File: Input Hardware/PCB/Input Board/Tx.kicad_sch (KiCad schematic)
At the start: 40 parts, among them U1001 TPIC6595, U1002 TPIC6595, U1003 TPIC6595, U1004 TPIC6595

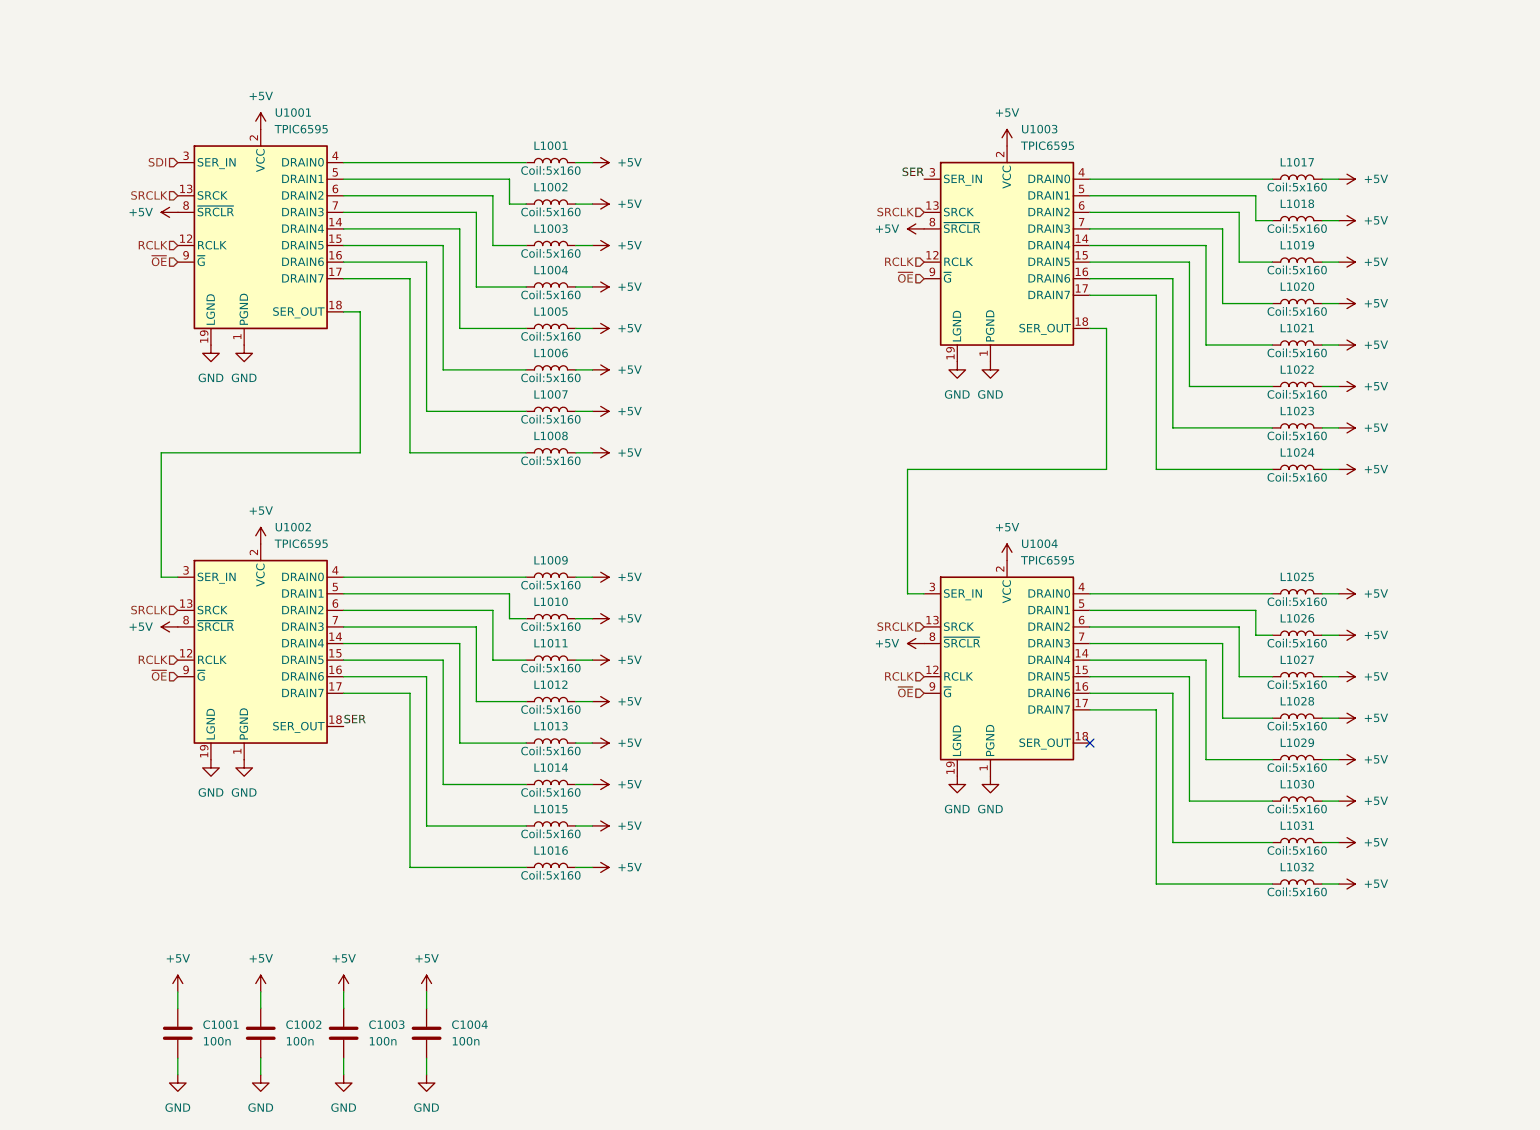
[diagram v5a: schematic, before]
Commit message: driver format update
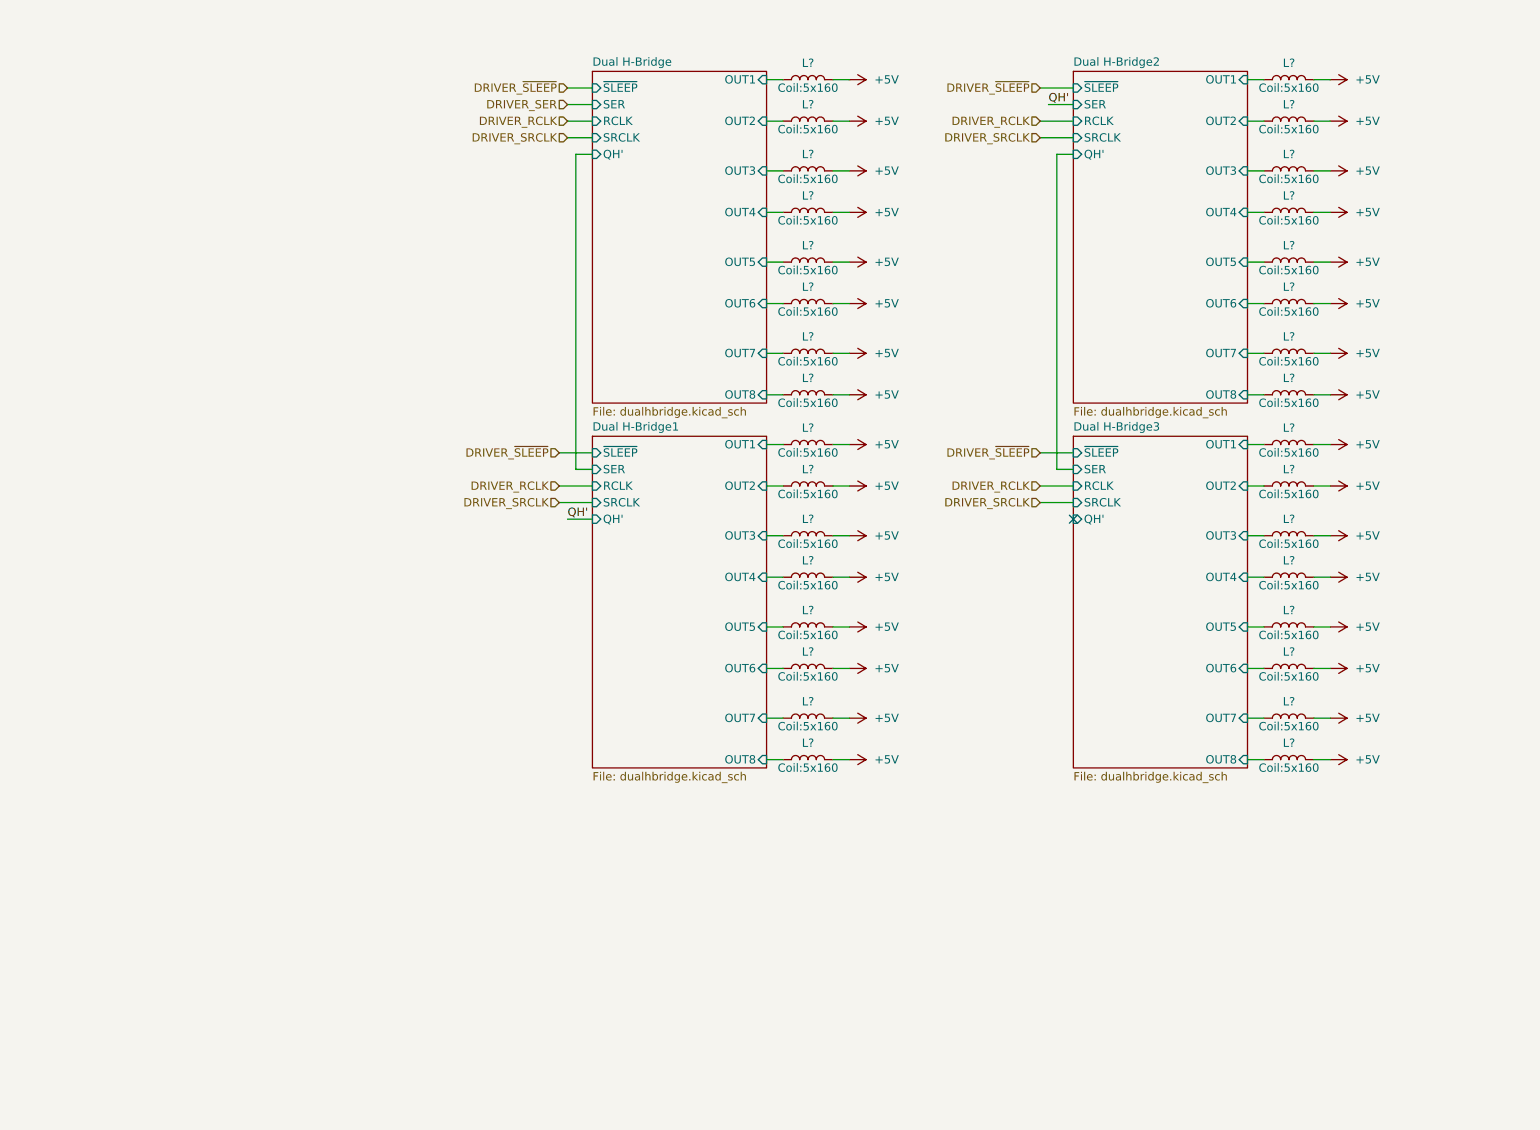
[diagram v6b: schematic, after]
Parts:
- removed C1001, C1002, C1003, C1004: 100n, Capacitor_SMD:C_0603_1608Metric, symbol Device:C
- removed U1001, U1002, U1003, U1004: TPIC6595, Package_SO:SOIC-20W_7.5x12.8mm_P1.27mm, symbol Interface_Expansion:TPIC6595
- renumbered L1019 to L?, L1024 to L?, L1006 to L?, L1003 to L?, L1008 to L?, L1027 to L?, L1007 to L?, L1030 to L?, L1026 to L?, L1004 to L?, L1013 to L?, L1014 to L?, L1011 to L?, L1017 to L?, L1010 to L?, L1031 to L?, L1002 to L?, L1001 to L?, L1005 to L?, L1020 to L?, L1015 to L?, L1023 to L?, L1016 to L?, L1022 to L?, L1018 to L?, L1029 to L?, L1025 to L?, L1028 to L?, L1012 to L?, L1032 to L?, L1009 to L?, L1021 to L?
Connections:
- net Dual H-Bridge2/OUT3: now reaches L?.1
- net Dual H-Bridge2/OUT8: now reaches L?.1
- net Dual H-Bridge/OUT6: now reaches L?.1
- net Dual H-Bridge/OUT3: now reaches L?.1
- net Dual H-Bridge/OUT8: now reaches L?.1
- net Dual H-Bridge3/OUT3: now reaches L?.1
- net Dual H-Bridge/OUT7: now reaches L?.1
- net Dual H-Bridge3/OUT6: now reaches L?.1
- net Dual H-Bridge3/OUT2: now reaches L?.1
- net Dual H-Bridge/OUT4: now reaches L?.1
- net Dual H-Bridge1/OUT5: now reaches L?.1
- net Dual H-Bridge1/OUT6: now reaches L?.1
- net Dual H-Bridge1/OUT3: now reaches L?.1
- net Dual H-Bridge2/OUT1: now reaches L?.1
- net Dual H-Bridge1/OUT2: now reaches L?.1
- net Dual H-Bridge3/OUT7: now reaches L?.1
- net Dual H-Bridge/OUT2: now reaches L?.1
- net Dual H-Bridge2/OUT5: now reaches L?.1
- net Dual H-Bridge2/OUT6: now reaches L?.1
- net Dual H-Bridge2/OUT7: now reaches L?.1
- net Dual H-Bridge2/OUT2: now reaches L?.1
- net Dual H-Bridge2/OUT4: now reaches L?.1
- net Dual H-Bridge/OUT1: now reaches L?.1
- net Dual H-Bridge/OUT5: now reaches L?.1
- net Dual H-Bridge1/OUT7: now reaches L?.1
- net Dual H-Bridge1/OUT8: now reaches L?.1
- net Dual H-Bridge1/OUT1: now reaches L?.1
- net Dual H-Bridge1/OUT4: now reaches L?.1
- net Dual H-Bridge3/OUT5: now reaches L?.1
- net Dual H-Bridge3/OUT8: now reaches L?.1
- net Dual H-Bridge3/OUT1: now reaches L?.1
- net Dual H-Bridge3/OUT4: now reaches L?.1
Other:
- added sheet Dual H-Bridge (dualhbridge.kicad_sch)
- added sheet Dual H-Bridge1 (dualhbridge.kicad_sch)
- added sheet Dual H-Bridge2 (dualhbridge.kicad_sch)
- added sheet Dual H-Bridge3 (dualhbridge.kicad_sch)
- moved on the sheet: L?
